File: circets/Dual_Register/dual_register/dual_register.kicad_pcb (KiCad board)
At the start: 2 copper layers, 111.8 x 205.7 mm, 23 parts, among them J1 Bus_Connector, J2 D_H, J3 D_L, J4 Conn_01x03_Male, U1 AM-Connector, U2 74HC573, U3 74HC573, U4 74HC573, U5 74HC573, U6 74HC573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

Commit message: Update Kicad to version 6 (and all of the schematics)
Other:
- net class Default: trace_width 0.5 -> 0.6

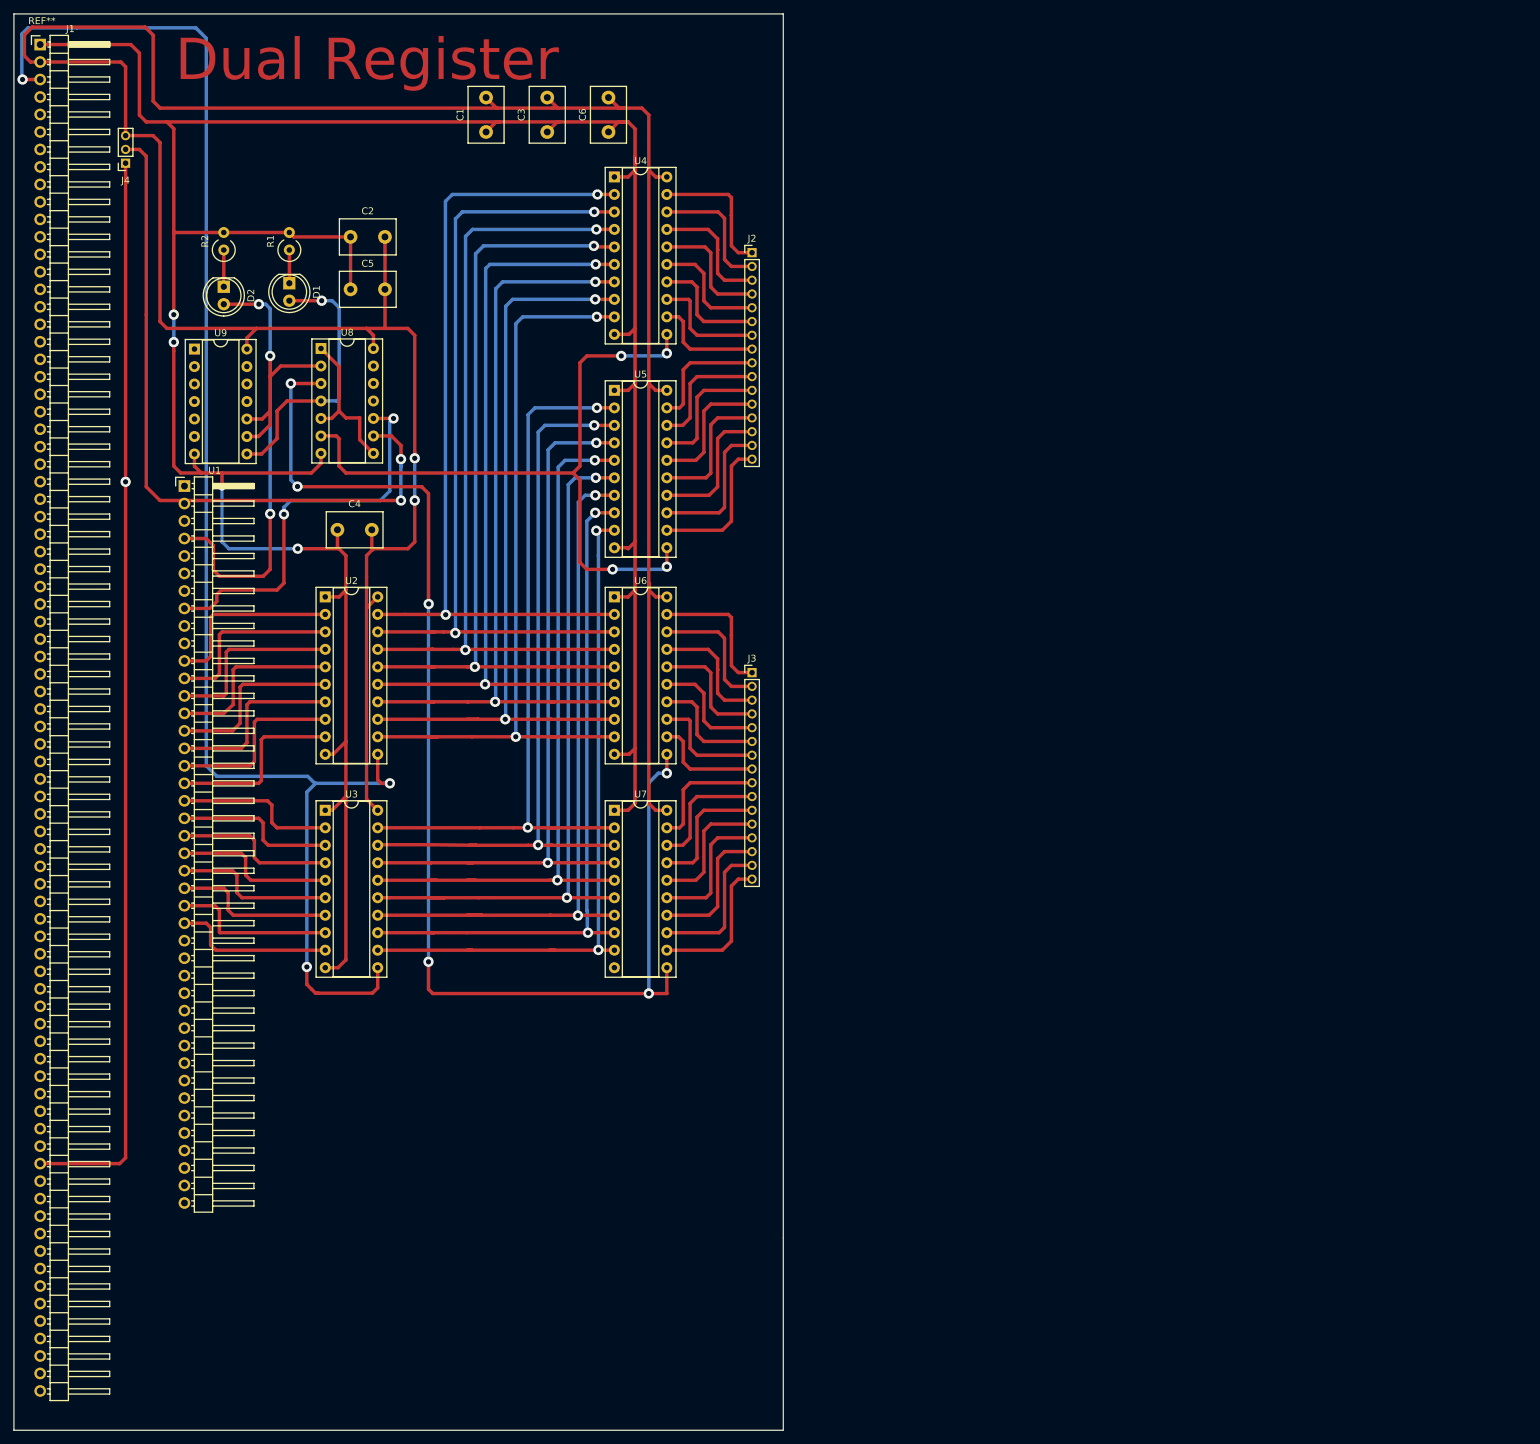
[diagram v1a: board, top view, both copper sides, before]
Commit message: Reworked PCB Layout for Dual Register
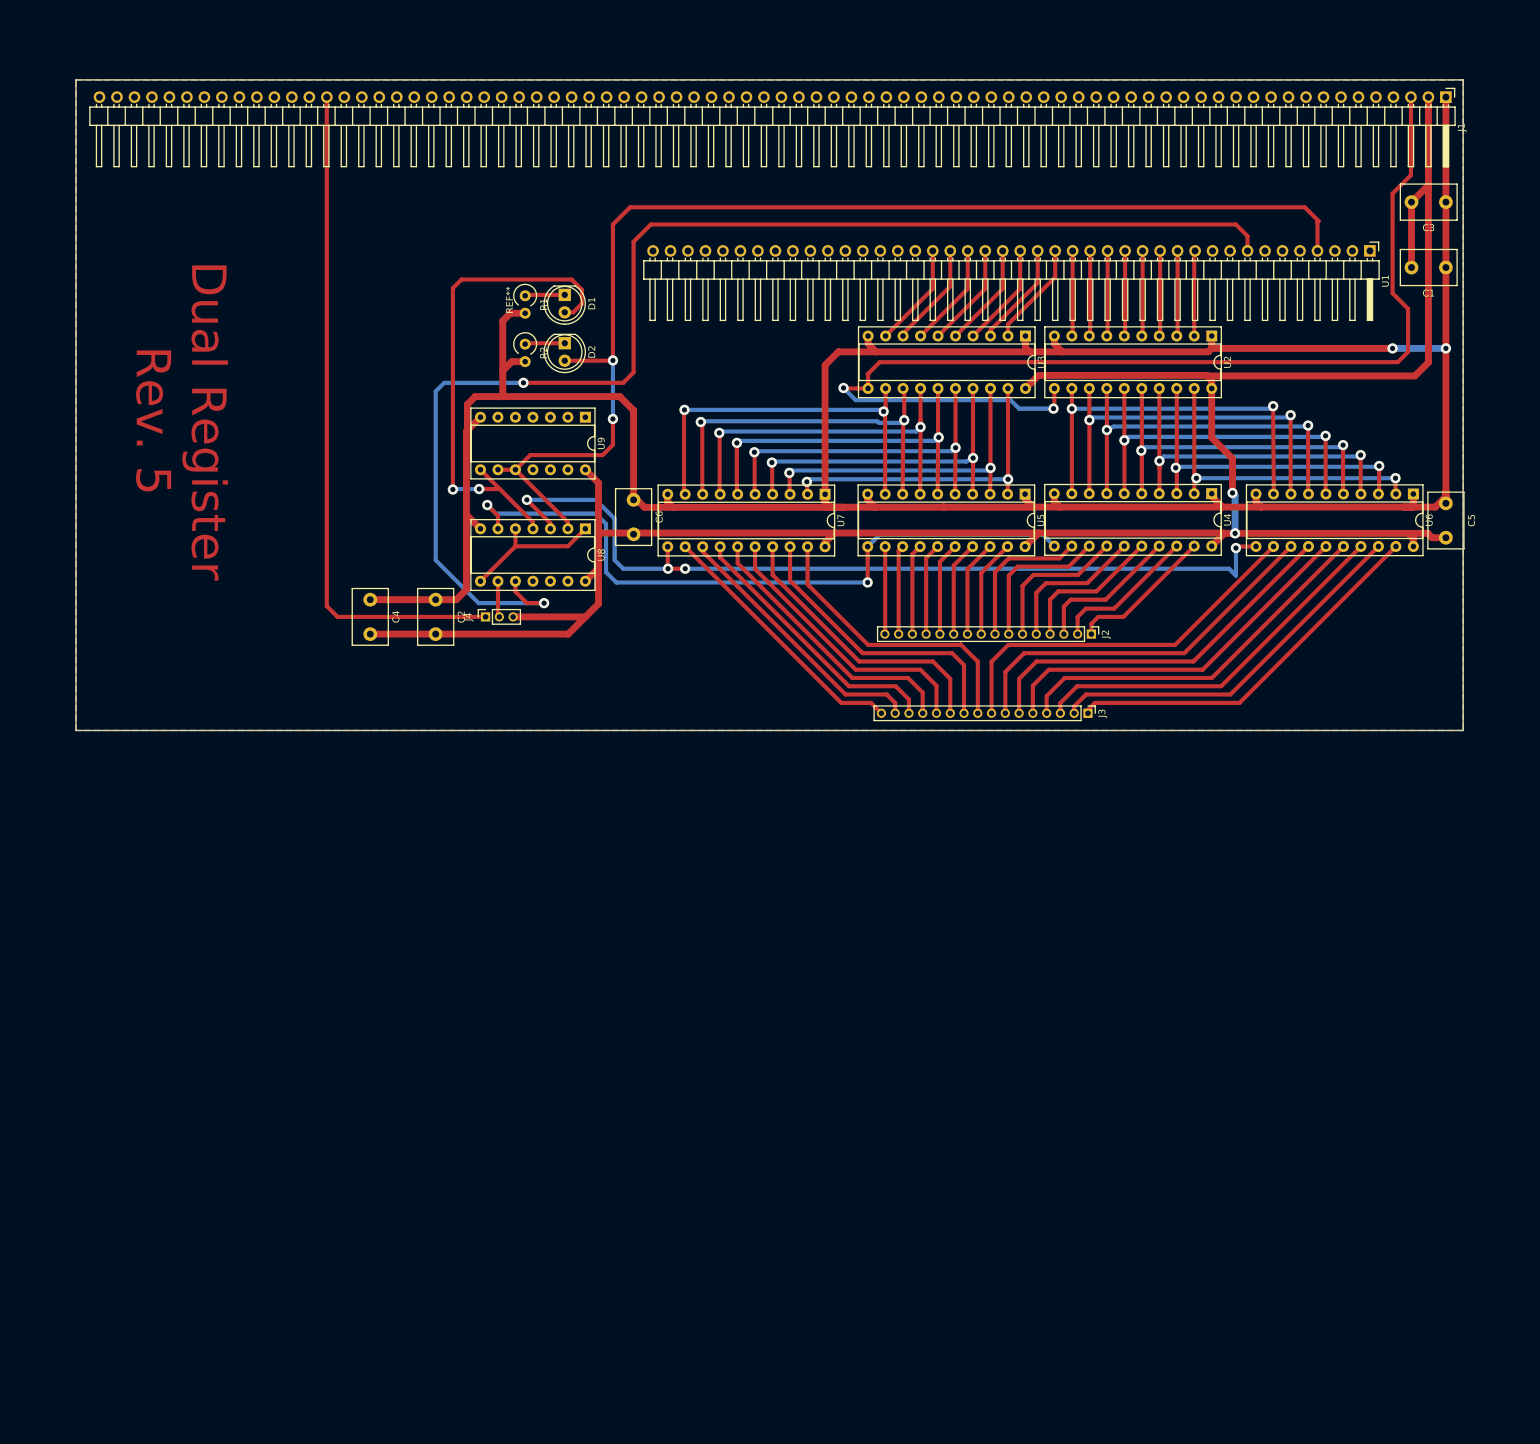
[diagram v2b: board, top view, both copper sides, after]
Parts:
- moved J1 204.3 mm to (220.7, 19.7), turned to -90 degrees
- moved U1 175.6 mm to (209.7, 42.0), turned to -90 degrees
- moved C5 162.1 mm to (220.7, 78.7), turned to -90 degrees
- moved C1 140.8 mm to (220.7, 44.5), turned to 180 degrees
- moved U2 134.2 mm to (186.7, 54.4), turned to -90 degrees
- moved C3 130.9 mm to (220.7, 35.0), turned to 180 degrees
- moved U3 122.9 mm to (159.6, 54.4), turned to -90 degrees
- moved U6 117.0 mm to (216.0, 77.4), turned to -90 degrees
- moved U4 98.2 mm to (186.7, 77.3), turned to -90 degrees
- moved J4 84.1 mm to (81.2, 95.2), turned to 90 degrees
- moved J2 74.2 mm to (169.2, 97.7), turned to -90 degrees
- moved U5 61.5 mm to (159.6, 77.4), turned to -90 degrees
- moved U9 57.6 mm to (95.7, 66.2), turned to -90 degrees
- moved U7 55.2 mm to (130.5, 77.4), turned to -90 degrees
- moved C2 54.1 mm to (74.0, 92.7), turned to -90 degrees
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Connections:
- J1 pad 4: Net-(J1-Pad4) -> unconnected-(J1-Pad4)
- J1 pad 66: Net-(J1-Pad66) -> unconnected-(J1-Pad66)
- J1 pad 67: Net-(J1-Pad67) -> unconnected-(J1-Pad67)
- U1 pad 1: Net-(U1-Pad1) -> unconnected-(U1-Pad1)
- U1 pad 2: Net-(U1-Pad2) -> unconnected-(U1-Pad2)
- U1 pad 3: Net-(U1-Pad3) -> unconnected-(U1-Pad3)
- U1 pad 5: Net-(U1-Pad5) -> unconnected-(U1-Pad5)
- U1 pad 6: Net-(U1-Pad6) -> unconnected-(U1-Pad6)
- U1 pad 7: Net-(U1-Pad7) -> unconnected-(U1-Pad7)
- U1 pad 9: Net-(U1-Pad9) -> unconnected-(U1-Pad9)
- U7 pad 10: Net-(U7-Pad10) -> GND
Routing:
- net Net-(U1-Pad8): track 57.6 -> 191.2 mm
- net Net-(J4-Pad2): track 101.8 -> 5.26 mm, vias 2 -> 0
- net Net-(D2-Pad2): track 88.1 -> 177.7 mm, vias 3 -> 2
- net +5V: track 421.2 -> 338.4 mm
- net Net-(U2-Pad19): track 120.1 -> 46.5 mm
- net Net-(U2-Pad18): track 118.8 -> 49.3 mm
- net Net-(U2-Pad17): track 117.0 -> 52.1 mm
- net Net-(U2-Pad16): track 116.7 -> 53.3 mm
- net Net-(U3-Pad19): track 108.3 -> 46.5 mm
- net Net-(J1-Pad3): track 220.0 -> 159.3 mm, vias 3 -> 2
- net Net-(U2-Pad15): track 114.7 -> 54.2 mm
- net Net-(J1-Pad65): track 157.2 -> 97.6 mm, vias 1 -> 0
- net Net-(U6-Pad11): track 186.4 -> 126.9 mm, vias 6 -> 4
- net Net-(U2-Pad14): track 113.6 -> 54.3 mm
- net Net-(U3-Pad18): track 107.2 -> 48.0 mm
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- added copper zone on B.Cu, net (none)
- added copper zone on F.Cu, net (none)
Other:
- board size 111.8 x 205.7 mm -> 201.5 x 94.5 mm
- net class Default removed
- board text added: "Dual Register Rev. 5"
- board text removed: "Dual Register"

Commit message: Added Name and other notest to AM PCB-Layout
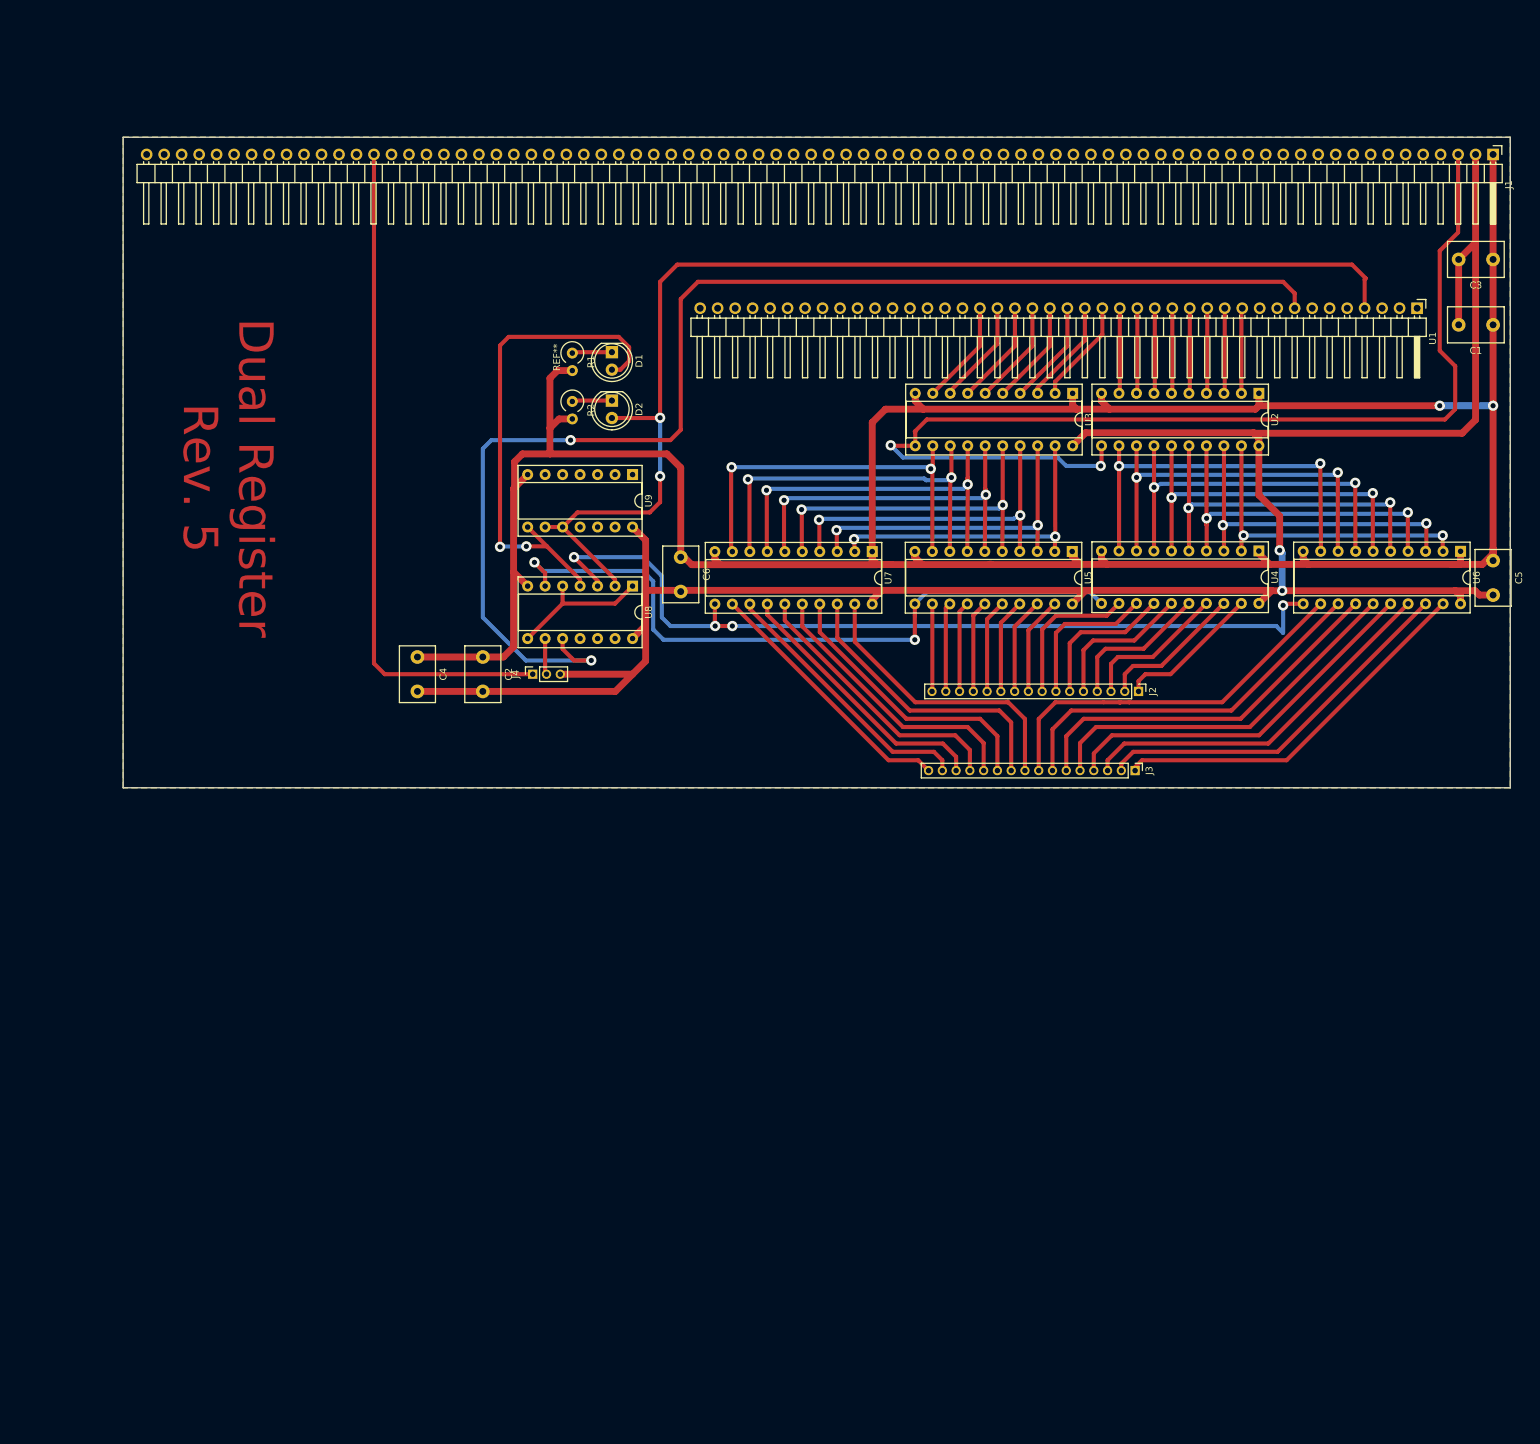
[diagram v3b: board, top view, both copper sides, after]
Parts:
- moved U5 10.8 mm to (166.4, 85.7)
- moved U3 10.8 mm to (166.5, 62.7)
- moved C2 10.8 mm to (80.8, 101.0)
- moved C4 10.8 mm to (71.3, 101.0)
- moved C6 10.8 mm to (109.6, 86.5)
- moved D1 10.8 mm to (99.6, 56.8)
- moved D2 10.8 mm to (99.6, 63.8)
- moved J4 10.8 mm to (88.1, 103.5)
- moved U8 10.8 mm to (102.6, 90.7)
- moved U9 10.8 mm to (102.6, 74.5)
- moved R1 10.8 mm to (93.8, 56.9)
- moved R2 10.8 mm to (93.8, 63.9)
- moved C1 10.8 mm to (227.6, 52.8)
- moved C3 10.8 mm to (227.6, 43.3)
- moved C5 10.8 mm to (227.6, 87.0)
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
